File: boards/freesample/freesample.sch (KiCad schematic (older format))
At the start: 7 parts, among them J1 SMA, J11 SMA, J12 SMA, J2 CONN_3_PWROUT

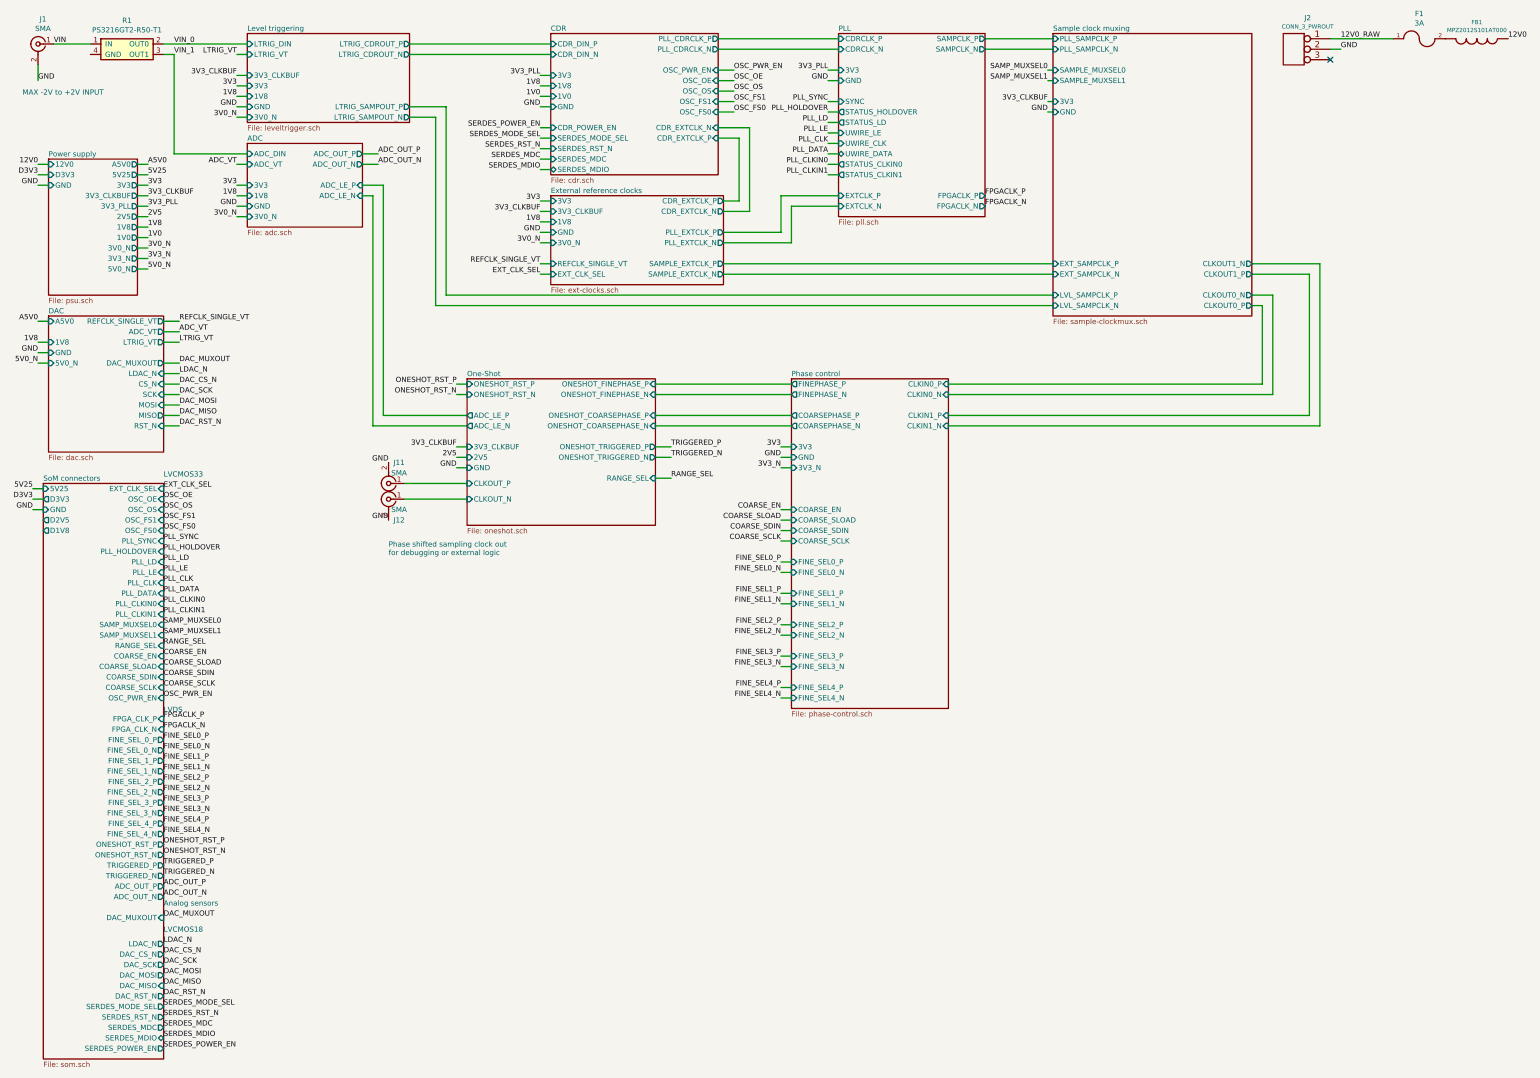
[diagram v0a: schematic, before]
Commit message: Added more test points. Started picking packages for passives. Continued schematic review.
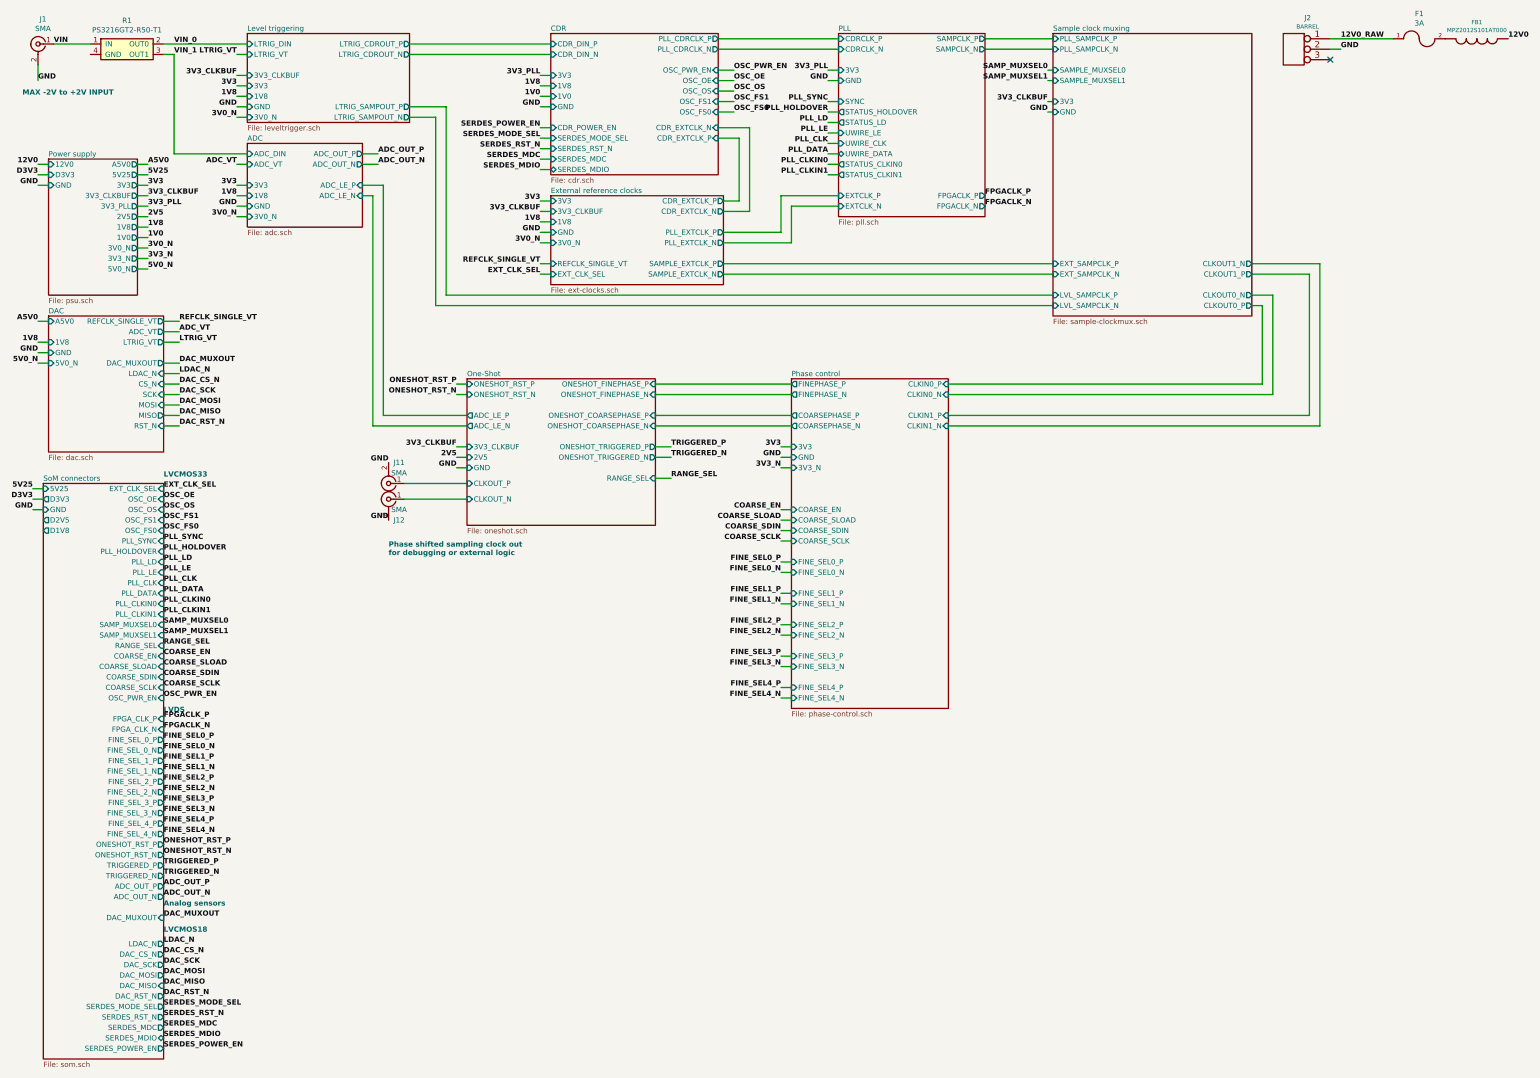
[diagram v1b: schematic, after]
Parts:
- F1: footprint (none) -> azonenberg_pcb:EIA_0603_RES_NOSILK
- FB1: footprint (none) -> azonenberg_pcb:EIA_0805_CAP_NOSILK
- J1, J11, J12: footprint (none) -> azonenberg_pcb:CONN_SMA_EDGE_SAMTEC_SMA_J_P_H_ST_EM1
- J2: value CONN_3_PWROUT -> BARREL; footprint (none) -> azonenberg_pcb:CONN_CUI_PJ-058BH_HIPWR_BARREL_NOSLOT

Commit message: Continued assigning footprints
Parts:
- added M1: TRACEPAD, azonenberg_pcb:SERIALNUM_MOLEX_0916580020, symbol Connector:Conn_01x01
- added M2: LOGO1, azonenberg_pcb:LONGTHING-1200DPI, symbol Connector:Conn_01x01
- added M3: LOGO2, w_logo:Logo_silk_OSHW_6x6mm, symbol Connector:Conn_01x01
- added M4: LOGO3, w_logo:Logo_silk_polarity_center_5x1.4mm, symbol Connector:Conn_01x01
- added M5: LOGO4, w_logo:Logo_silk_ROHS_5x2.8mm, symbol Connector:Conn_01x01
- added M6: LOGO5, w_logo:Logo_silk_warning_5x4.2mm, symbol Connector:Conn_01x01
- added M7: LOGO6, w_logo:Logo_silk_WEEE_3.4x5mm, symbol Connector:Conn_01x01
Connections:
- no-connect marks 1 -> 8
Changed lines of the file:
@@
 Sheet 1 12
 Title "FREESAMPLE Oscilloscope"
-Date "2019-03-15"
+Date "2019-03-16"
 Rev "0.1"
 Comp "Andrew D. Zonenberg / Antikernel Labs"
@@
 Text Notes 4100 5750 0    50   ~ 6
 Phase shifted sampling clock out\nfor debugging or external logic
+$Comp
+L Connector:Conn_01x01 M1
+U 1 1 5CAB1898
+P 15150 1500
+F 0 "M1" H 15068 1275 50  0000 C CNN
+F 1 "TRACEPAD" H 15068 1366 50  0000 C CNN
+F 2 "azonenberg_pcb:SERIALNUM_MOLEX_0916580020" H 15150 1500 50  0001 C CNN
+F 3 "~" H 15150 1500 50  0001 C CNN
+	1    15150 1500
+	-1   0    0    1
+$EndComp
+NoConn ~ 15350 1500
+$Comp
+L Connector:Conn_01x01 M2
+U 1 1 5CABDA7C
+P 15150 1850
+F 0 "M2" H 15068 1625 50  0000 C CNN
+F 1 "LOGO1" H 15068 1716 50  0000 C CNN
+F 2 "azonenberg_pcb:LONGTHING-1200DPI" H 15150 1850 50  0001 C CNN
+F 3 "~" H 15150 1850 50  0001 C CNN
+	1    15150 1850
+	-1   0    0    1
+$EndComp
+NoConn ~ 15350 1850
+$Comp
+L Connector:Conn_01x01 M3
+U 1 1 5CAC9CF3
+P 15150 2200
+F 0 "M3" H 15068 1975 50  0000 C CNN
+F 1 "LOGO2" H 15068 2066 50  0000 C CNN
+F 2 "w_logo:Logo_silk_OSHW_6x6mm" H 15150 2200 50  0001 C CNN
+F 3 "~" H 15150 2200 50  0001 C CNN
+	1    15150 2200
+	-1   0    0    1
+$EndComp
+NoConn ~ 15350 2200
+$Comp
+L Connector:Conn_01x01 M4
+U 1 1 5CADB0C0
+P 15150 2550
+F 0 "M4" H 15068 2325 50  0000 C CNN
+F 1 "LOGO3" H 15068 2416 50  0000 C CNN
+F 2 "w_logo:Logo_silk_polarity_center_5x1.4mm" H 15150 2550 50  0001 C CNN
+F 3 "~" H 15150 2550 50  0001 C CNN
+	1    15150 2550
+	-1   0    0    1
+$EndComp
+NoConn ~ 15350 2550
+$Comp
+L Connector:Conn_01x01 M5
+U 1 1 5CADB0CB
+P 15150 2900
+F 0 "M5" H 15068 2675 50  0000 C CNN
+F 1 "LOGO4" H 15068 2766 50  0000 C CNN
+F 2 "w_logo:Logo_silk_ROHS_5x2.8mm" H 15150 2900 50  0001 C CNN
+F 3 "~" H 15150 2900 50  0001 C CNN
+	1    15150 2900
+	-1   0    0    1
+$EndComp
+NoConn ~ 15350 2900
+$Comp
+L Connector:Conn_01x01 M6
+U 1 1 5CAED480
+P 15150 3250
+F 0 "M6" H 15068 3025 50  0000 C CNN
+F 1 "LOGO5" H 15068 3116 50  0000 C CNN
+F 2 "w_logo:Logo_silk_warning_5x4.2mm" H 15150 3250 50  0001 C CNN
+F 3 "~" H 15150 3250 50  0001 C CNN
+	1    15150 3250
+	-1   0    0    1
+$EndComp
+NoConn ~ 15350 3250
+$Comp
+L Connector:Conn_01x01 M7
+U 1 1 5CAED48B
+P 15150 3600
+F 0 "M7" H 15068 3375 50  0000 C CNN
+F 1 "LOGO6" H 15068 3466 50  0000 C CNN
+F 2 "w_logo:Logo_silk_WEEE_3.4x5mm" H 15150 3600 50  0001 C CNN
+F 3 "~" H 15150 3600 50  0001 C CNN
+	1    15150 3600
+	-1   0    0    1
+$EndComp
+NoConn ~ 15350 3600
 $EndSCHEMATC

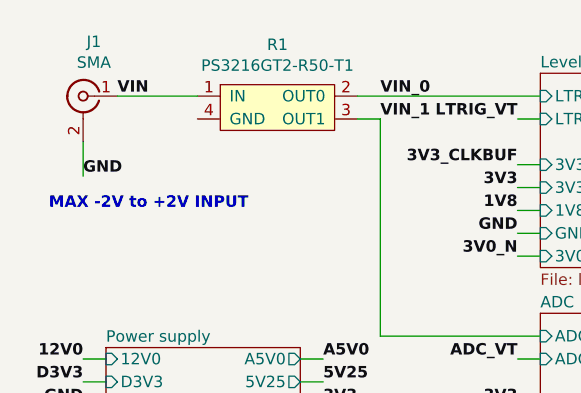
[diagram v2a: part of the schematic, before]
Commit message: Continued selecting component footprints and working on schematic review
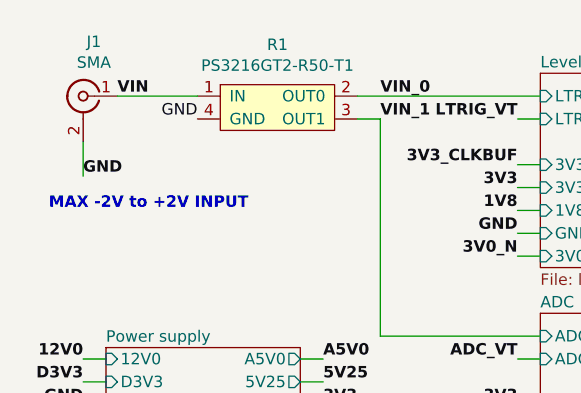
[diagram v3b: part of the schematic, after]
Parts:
- R1: footprint (none) -> azonenberg_pcb:SPLITTER_SUSUMU_PS3216G
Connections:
- net GND: now also R1.4 (GND)
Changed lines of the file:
@@
 F 0 "R1" H 1600 1375 50  0000 C CNN
 F 1 "PS3216GT2-R50-T1‎" H 1600 1284 50  0000 C CNN
-F 2 "" H 1350 1000 50  0001 C CNN
+F 2 "azonenberg_pcb:SPLITTER_SUSUMU_PS3216G" H 1350 1000 50  0001 C CNN
 F 3 "" H 1350 1000 50  0001 C CNN
 	1    1350 1000
@@
 $EndComp
 NoConn ~ 15350 3600
+Text Label 1250 950  2    50   ~ 0
+GND
 $EndSCHEMATC

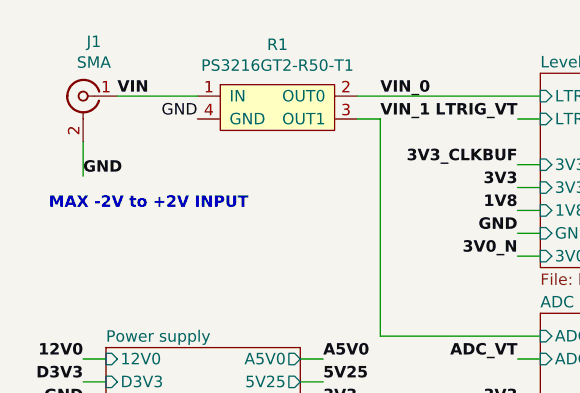
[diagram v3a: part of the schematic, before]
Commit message: Continued schematic review. Significantly simplified one-shot to reduce jitter, board area, and power consumption
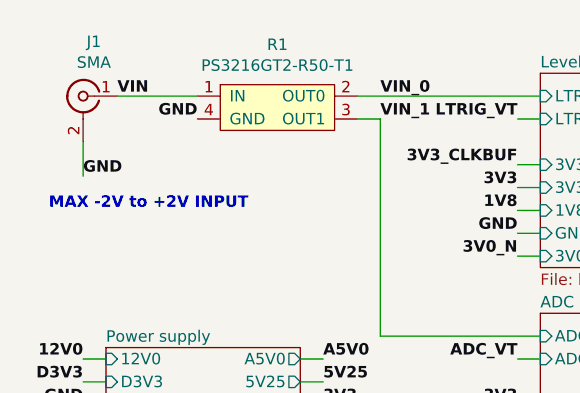
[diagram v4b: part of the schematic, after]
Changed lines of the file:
@@
 $EndComp
 NoConn ~ 15350 3600
-Text Label 1250 950  2    50   ~ 0
+Text Label 1250 950  2    50   ~ 6
 GND
 $EndSCHEMATC

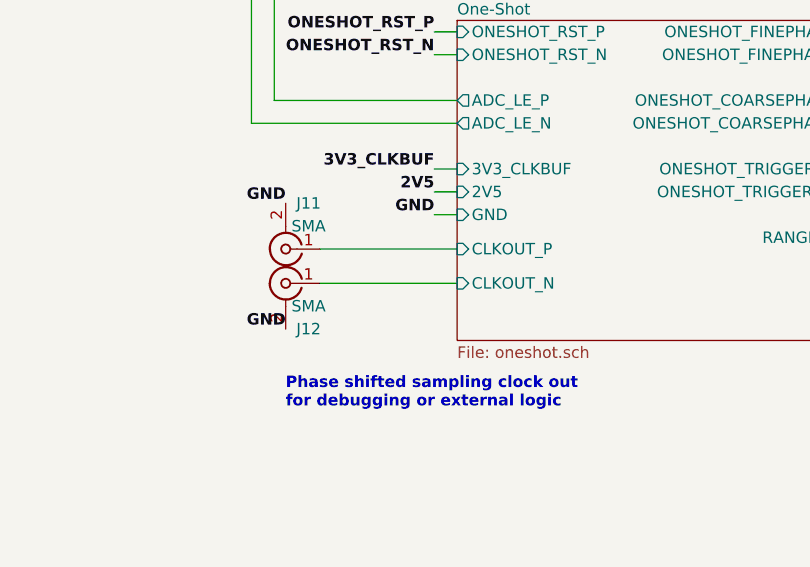
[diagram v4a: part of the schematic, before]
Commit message: Continued design review. Changed termination on DFFs to 1V8. Added some pull resistors to keep DFFs in reset during boot.
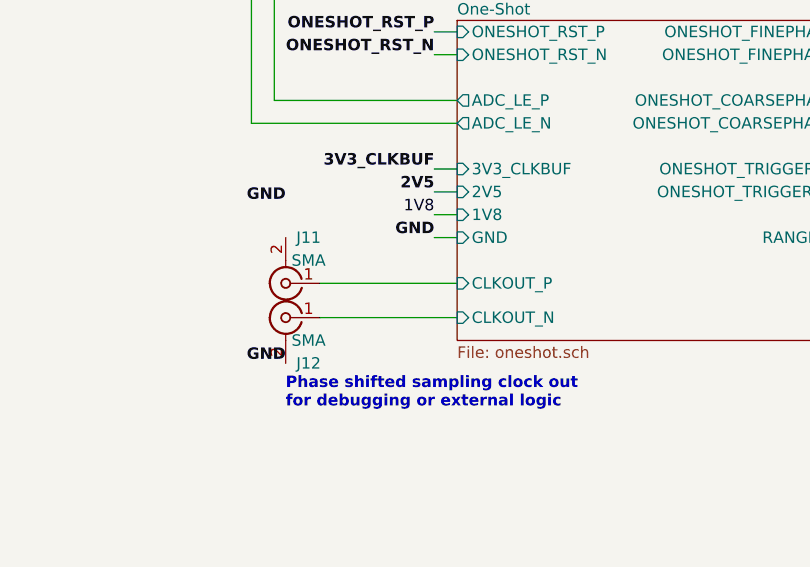
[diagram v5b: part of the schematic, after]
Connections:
- net GND: no longer J11.2 (Ext)
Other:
- moved on the sheet: J11, J12
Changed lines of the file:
@@
 Sheet 1 12
 Title "FREESAMPLE Oscilloscope"
-Date "2019-03-16"
+Date "2019-03-17"
 Rev "0.1"
 Comp "Andrew D. Zonenberg / Antikernel Labs"
@@
 F4 "ONESHOT_RST_P" I L 4850 4100 50
 F5 "ONESHOT_RST_N" I L 4850 4200 50
-F6 "GND" I L 4850 4900 50
+F6 "GND" I L 4850 5000 50
 F7 "ONESHOT_TRIGGERED_P" O R 6650 4700 50
 F8 "ONESHOT_TRIGGERED_N" O R 6650 4800 50
@@
 F14 "2V5" I L 4850 4800 50
 F15 "3V3_CLKBUF" I L 4850 4700 50
-F16 "CLKOUT_P" I L 4850 5050 50
-F17 "CLKOUT_N" I L 4850 5200 50
+F16 "CLKOUT_P" I L 4850 5200 50
+F17 "CLKOUT_N" I L 4850 5350 50
+F18 "1V8" I L 4850 4900 50
 $EndSheet
 $Comp
@@
 Wire Wire Line
 	4750 4900 4850 4900
-Text Label 4750 4900 2    50   ~ 6
+Text Label 4750 5000 2    50   ~ 6
 GND
 Text Label 4750 4800 2    50   ~ 6
@@
 L Connector:Conn_Coaxial J12
 U 1 1 5D23CAB3
+P 4100 5350
+F 0 "J12" H 4000 5150 50  0000 C CNN
+F 1 "SMA" H 4000 5250 50  0000 C CNN
+F 2 "azonenberg_pcb:CONN_SMA_EDGE_SAMTEC_SMA_J_P_H_ST_EM1" H 4100 5350 50  0001 C CNN
+F 3 "" H 4100 5350 50  0001 C CNN
+	1    4100 5350
+	-1   0    0    -1
+$EndComp
+$Comp
+L Connector:Conn_Coaxial J11
+U 1 1 5D23D75B
 P 4100 5200
-F 0 "J12" H 4000 5000 50  0000 C CNN
+F 0 "J11" H 4000 5000 50  0000 C CNN
 F 1 "SMA" H 4000 5100 50  0000 C CNN
 F 2 "azonenberg_pcb:CONN_SMA_EDGE_SAMTEC_SMA_J_P_H_ST_EM1" H 4100 5200 50  0001 C CNN
 F 3 "" H 4100 5200 50  0001 C CNN
 	1    4100 5200
-	-1   0    0    -1
-$EndComp
-$Comp
-L Connector:Conn_Coaxial J11
-U 1 1 5D23D75B
-P 4100 5050
-F 0 "J11" H 4000 4850 50  0000 C CNN
-F 1 "SMA" H 4000 4950 50  0000 C CNN
-F 2 "azonenberg_pcb:CONN_SMA_EDGE_SAMTEC_SMA_J_P_H_ST_EM1" H 4100 5050 50  0001 C CNN
-F 3 "" H 4100 5050 50  0001 C CNN
-	1    4100 5050
 	-1   0    0    1
 $EndComp
 Wire Wire Line
-	4850 5200 4250 5200
+	4850 5350 4250 5350
 Text Label 4100 4850 2    50   ~ 6
 GND
-Text Label 4100 5400 2    50   ~ 6
-GND
-Wire Wire Line
-	4250 5050 4850 5050
+Text Label 4100 5550 2    50   ~ 6
+GND
+Wire Wire Line
+	4250 5200 4850 5200
 Text Notes 4100 5750 0    50   ~ 6
 Phase shifted sampling clock out\nfor debugging or external logic
@@
 Text Label 1250 950  2    50   ~ 6
 GND
+Text Label 4750 4900 2    50   ~ 0
+1V8
+Wire Wire Line
+	4750 5000 4850 5000
 $EndSCHEMATC

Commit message: Added fiducials
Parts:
- added FID1, FID2, FID3, FID4, FID5, FID6: FIDUCIAL, azonenberg_pcb:FIDUCIAL_1MM, symbol special-azonenberg:MECHANICAL
- M1, M2, M3, M4, M5, M6, M7: symbol Connector:Conn_01x01 -> special-azonenberg:MECHANICAL
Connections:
- net GND: now also J11.2 (Ext)
- no-connect marks 8 -> 1
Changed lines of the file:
@@
 Wire Wire Line
 	4850 5350 4250 5350
-Text Label 4100 4850 2    50   ~ 6
+Text Label 4100 5000 2    50   ~ 6
 GND
 Text Label 4100 5550 2    50   ~ 6
@@
 Phase shifted sampling clock out\nfor debugging or external logic
 $Comp
-L Connector:Conn_01x01 M1
+L special-azonenberg:MECHANICAL M1
 U 1 1 5CAB1898
 P 15150 1500
-F 0 "M1" H 15068 1275 50  0000 C CNN
-F 1 "TRACEPAD" H 15068 1366 50  0000 C CNN
+F 0 "M1" H 15122 1454 50  0000 R CNN
+F 1 "TRACEPAD" H 15122 1545 50  0000 R CNN
 F 2 "azonenberg_pcb:SERIALNUM_MOLEX_0916580020" H 15150 1500 50  0001 C CNN
 F 3 "~" H 15150 1500 50  0001 C CNN
@@
 	-1   0    0    1
 $EndComp
-NoConn ~ 15350 1500
 $Comp
-L Connector:Conn_01x01 M2
+L special-azonenberg:MECHANICAL M2
 U 1 1 5CABDA7C
 P 15150 1850
-F 0 "M2" H 15068 1625 50  0000 C CNN
-F 1 "LOGO1" H 15068 1716 50  0000 C CNN
+F 0 "M2" H 15122 1804 50  0000 R CNN
+F 1 "LOGO1" H 15122 1895 50  0000 R CNN
 F 2 "azonenberg_pcb:LONGTHING-1200DPI" H 15150 1850 50  0001 C CNN
 F 3 "~" H 15150 1850 50  0001 C CNN
@@
 	-1   0    0    1
 $EndComp
-NoConn ~ 15350 1850
 $Comp
-L Connector:Conn_01x01 M3
+L special-azonenberg:MECHANICAL M3
 U 1 1 5CAC9CF3
 P 15150 2200
-F 0 "M3" H 15068 1975 50  0000 C CNN
-F 1 "LOGO2" H 15068 2066 50  0000 C CNN
+F 0 "M3" H 15122 2154 50  0000 R CNN
+F 1 "LOGO2" H 15122 2245 50  0000 R CNN
 F 2 "w_logo:Logo_silk_OSHW_6x6mm" H 15150 2200 50  0001 C CNN
 F 3 "~" H 15150 2200 50  0001 C CNN
@@
 	-1   0    0    1
 $EndComp
-NoConn ~ 15350 2200
 $Comp
-L Connector:Conn_01x01 M4
+L special-azonenberg:MECHANICAL M4
 U 1 1 5CADB0C0
 P 15150 2550
-F 0 "M4" H 15068 2325 50  0000 C CNN
-F 1 "LOGO3" H 15068 2416 50  0000 C CNN
+F 0 "M4" H 15122 2504 50  0000 R CNN
+F 1 "LOGO3" H 15122 2595 50  0000 R CNN
 F 2 "w_logo:Logo_silk_polarity_center_5x1.4mm" H 15150 2550 50  0001 C CNN
 F 3 "~" H 15150 2550 50  0001 C CNN
@@
 	-1   0    0    1
 $EndComp
-NoConn ~ 15350 2550
 $Comp
-L Connector:Conn_01x01 M5
+L special-azonenberg:MECHANICAL M5
 U 1 1 5CADB0CB
 P 15150 2900
-F 0 "M5" H 15068 2675 50  0000 C CNN
-F 1 "LOGO4" H 15068 2766 50  0000 C CNN
+F 0 "M5" H 15122 2854 50  0000 R CNN
+F 1 "LOGO4" H 15122 2945 50  0000 R CNN
 F 2 "w_logo:Logo_silk_ROHS_5x2.8mm" H 15150 2900 50  0001 C CNN
 F 3 "~" H 15150 2900 50  0001 C CNN
@@
 	-1   0    0    1
 $EndComp
-NoConn ~ 15350 2900
 $Comp
-L Connector:Conn_01x01 M6
+L special-azonenberg:MECHANICAL M6
 U 1 1 5CAED480
 P 15150 3250
-F 0 "M6" H 15068 3025 50  0000 C CNN
-F 1 "LOGO5" H 15068 3116 50  0000 C CNN
+F 0 "M6" H 15122 3204 50  0000 R CNN
+F 1 "LOGO5" H 15122 3295 50  0000 R CNN
 F 2 "w_logo:Logo_silk_warning_5x4.2mm" H 15150 3250 50  0001 C CNN
 F 3 "~" H 15150 3250 50  0001 C CNN
@@
 	-1   0    0    1
 $EndComp
-NoConn ~ 15350 3250
 $Comp
-L Connector:Conn_01x01 M7
+L special-azonenberg:MECHANICAL M7
 U 1 1 5CAED48B
 P 15150 3600
-F 0 "M7" H 15068 3375 50  0000 C CNN
-F 1 "LOGO6" H 15068 3466 50  0000 C CNN
+F 0 "M7" H 15122 3554 50  0000 R CNN
+F 1 "LOGO6" H 15122 3645 50  0000 R CNN
 F 2 "w_logo:Logo_silk_WEEE_3.4x5mm" H 15150 3600 50  0001 C CNN
 F 3 "~" H 15150 3600 50  0001 C CNN
@@
 	-1   0    0    1
 $EndComp
-NoConn ~ 15350 3600
 Text Label 1250 950  2    50   ~ 6
 GND
-Text Label 4750 4900 2    50   ~ 0
+Text Label 4750 4900 2    50   ~ 6
 1V8
 Wire Wire Line
 	4750 5000 4850 5000
+$Comp
+L special-azonenberg:MECHANICAL FID1
+U 1 1 5D1D857C
+P 15150 3900
+F 0 "FID1" H 15122 3854 50  0000 R CNN
+F 1 "FIDUCIAL" H 15122 3945 50  0000 R CNN
+F 2 "azonenberg_pcb:FIDUCIAL_1MM" H 15150 3900 50  0001 C CNN
+F 3 "~" H 15150 3900 50  0001 C CNN
+	1    15150 3900
+	-1   0    0    1
+$EndComp
+$Comp
+L special-azonenberg:MECHANICAL FID2
+U 1 1 5D1F082F
+P 15150 4200
+F 0 "FID2" H 15122 4154 50  0000 R CNN
+F 1 "FIDUCIAL" H 15122 4245 50  0000 R CNN
+F 2 "azonenberg_pcb:FIDUCIAL_1MM" H 15150 4200 50  0001 C CNN
+F 3 "~" H 15150 4200 50  0001 C CNN
+	1    15150 4200
+	-1   0    0    1
+$EndComp
+$Comp
+L special-azonenberg:MECHANICAL FID3
+U 1 1 5D1FCA39
+P 15150 4500
+F 0 "FID3" H 15122 4454 50  0000 R CNN
+F 1 "FIDUCIAL" H 15122 4545 50  0000 R CNN
+F 2 "azonenberg_pcb:FIDUCIAL_1MM" H 15150 4500 50  0001 C CNN
+F 3 "~" H 15150 4500 50  0001 C CNN
+	1    15150 4500
+	-1   0    0    1
+$EndComp
+$Comp
+L special-azonenberg:MECHANICAL FID4
+U 1 1 5D1FCA43
+P 15150 4800
+F 0 "FID4" H 15122 4754 50  0000 R CNN
+F 1 "FIDUCIAL" H 15122 4845 50  0000 R CNN
+F 2 "azonenberg_pcb:FIDUCIAL_1MM" H 15150 4800 50  0001 C CNN
+F 3 "~" H 15150 4800 50  0001 C CNN
+	1    15150 4800
+	-1   0    0    1
+$EndComp
+$Comp
+L special-azonenberg:MECHANICAL FID5
+U 1 1 5D215225
+P 15150 5100
+F 0 "FID5" H 15122 5054 50  0000 R CNN
+F 1 "FIDUCIAL" H 15122 5145 50  0000 R CNN
+F 2 "azonenberg_pcb:FIDUCIAL_1MM" H 15150 5100 50  0001 C CNN
+F 3 "~" H 15150 5100 50  0001 C CNN
+	1    15150 5100
+	-1   0    0    1
+$EndComp
+$Comp
+L special-azonenberg:MECHANICAL FID6
+U 1 1 5D21522F
+P 15150 5400
+F 0 "FID6" H 15122 5354 50  0000 R CNN
+F 1 "FIDUCIAL" H 15122 5445 50  0000 R CNN
+F 2 "azonenberg_pcb:FIDUCIAL_1MM" H 15150 5400 50  0001 C CNN
+F 3 "~" H 15150 5400 50  0001 C CNN
+	1    15150 5400
+	-1   0    0    1
+$EndComp
 $EndSCHEMATC
